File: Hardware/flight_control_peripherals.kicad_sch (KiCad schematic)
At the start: 17 parts, among them J10 Conn_02x06_Odd_Even, J11 Conn_01x06, J12 Micro_SD_Card_Det1, J6 Conn_01x10, J7 Conn_02x10_Odd_Even, J8 Conn_01x04, J9 Conn_01x04, U13 W25N01GVZEIG_TR, U14 24CW1280T-I/OT, U15 PCA9685PW_118

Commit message: firmware started, freertos, initial sensors abstractions, some pin layout changes
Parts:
- U14: footprint SOT-23-5_2P9X1P6_MCH -> (none)
- U15: footprint TSSOP28_SOT361-1_NXP -> (none)
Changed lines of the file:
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@@
 			)
 		)
-		(property "Footprint" "TSSOP28_SOT361-1_NXP"
+		(property "Footprint" ""
 			(at 212.09 41.91 0)
 			(effects
@@
 			)
 		)
-		(property "Footprint" "SOT-23-5_2P9X1P6_MCH"
+		(property "Footprint" ""
 			(at 85.09 158.75 0)
 			(effects

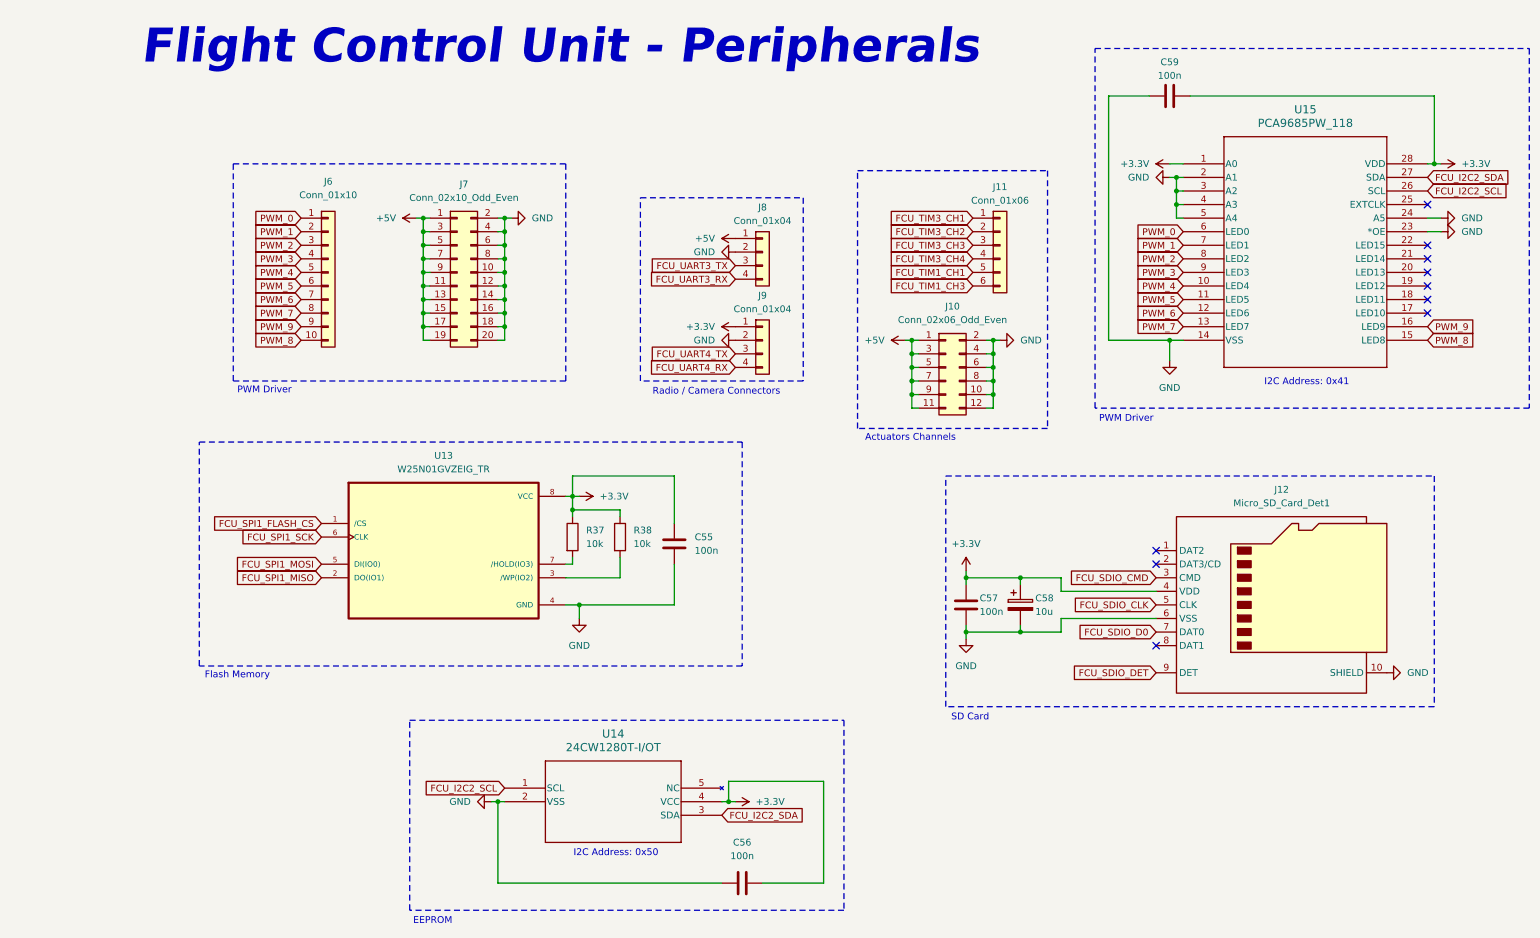
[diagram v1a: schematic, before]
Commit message: add some footprints, and pcb configs
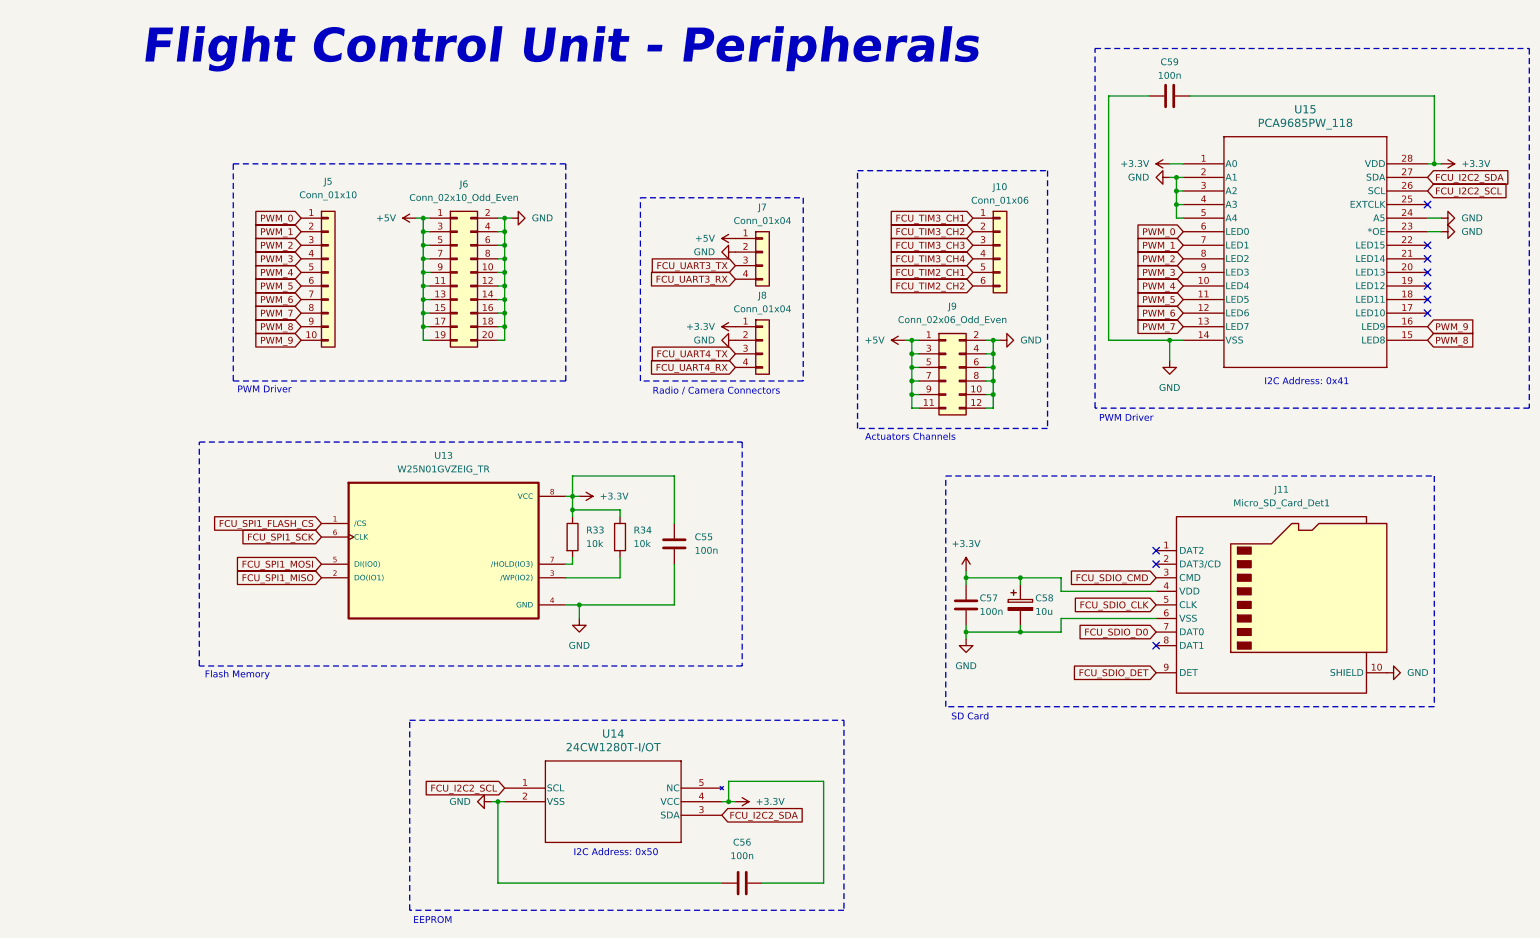
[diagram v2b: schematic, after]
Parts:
- C55, C56, C57, C59: footprint (none) -> Capacitor_SMD:C_0603_1608Metric
- C58: footprint (none) -> Capacitor_Tantalum_SMD:CP_EIA-1608-08_AVX-J
- U14: footprint (none) -> Aircraft_Footprints:SOT-23-5_2P9X1P6_MCH
- U15: footprint (none) -> Aircraft_Footprints:TSSOP28_SOT361-1_NXP
- renumbered J11 to J10, J12 to J11, J6 to J5, J7 to J6, J8 to J7, J9 to J8, J10 to J9, R37 to R33, R38 to R34
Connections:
- net PWM_8: now also J5.9 (Pin_9); no longer J5.10 (Pin_10)
- net PWM_9: now also J5.10 (Pin_10); no longer J5.9 (Pin_9)
- net FCU_TIM1_CH1 renamed FCU_TIM2_CH1
- net FCU_TIM1_CH3 renamed FCU_TIM2_CH2
